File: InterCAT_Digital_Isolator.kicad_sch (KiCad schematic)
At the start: 22 parts, among them U10 MAX3250, U11 EL357N(C)(TA)-G, U12 EL357N(C)(TA)-G, U8 EL357N(C)(TA)-G, U9 EL357N(C)(TA)-G

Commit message: corrected gain of the amplifiers and dyn range, continued PCB
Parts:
- C27, C32: Note X7R -> 50V X7R
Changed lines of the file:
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@@
       (effects (font (size 1.27 1.27)) hide)
     )
-    (property "Note" "X7R" (at 149.86 30.48 0)
+    (property "Note" "50V X7R" (at 149.86 30.48 0)
       (effects (font (size 1.27 1.27)) hide)
     )
@@
       (effects (font (size 1.27 1.27)) hide)
     )
-    (property "Note" "X7R" (at 154.94 30.48 0)
-      (effects (font (size 1.27 1.27)) hide)
-    )
+    (property "Note" "50V X7R" (at 154.94 30.48 0)
+      (effects (font (size 1.27 1.27)) hide)
+    )

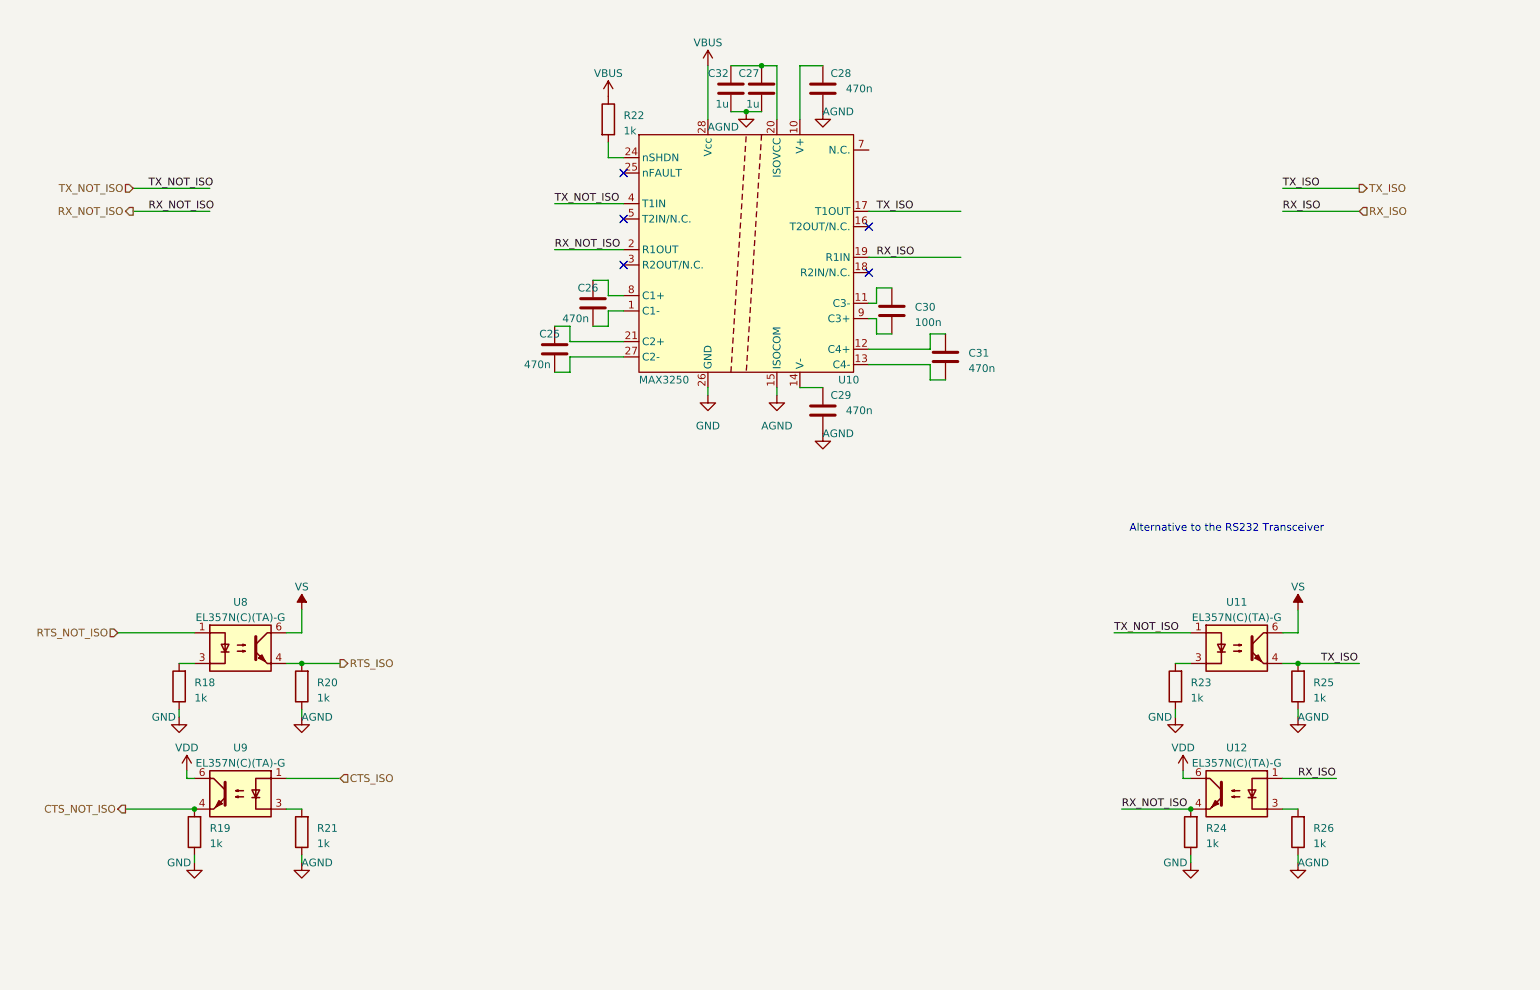
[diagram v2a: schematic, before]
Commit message: Started Version 2.0, migrated to STM32, changed some symbols, added 3V3 Supply
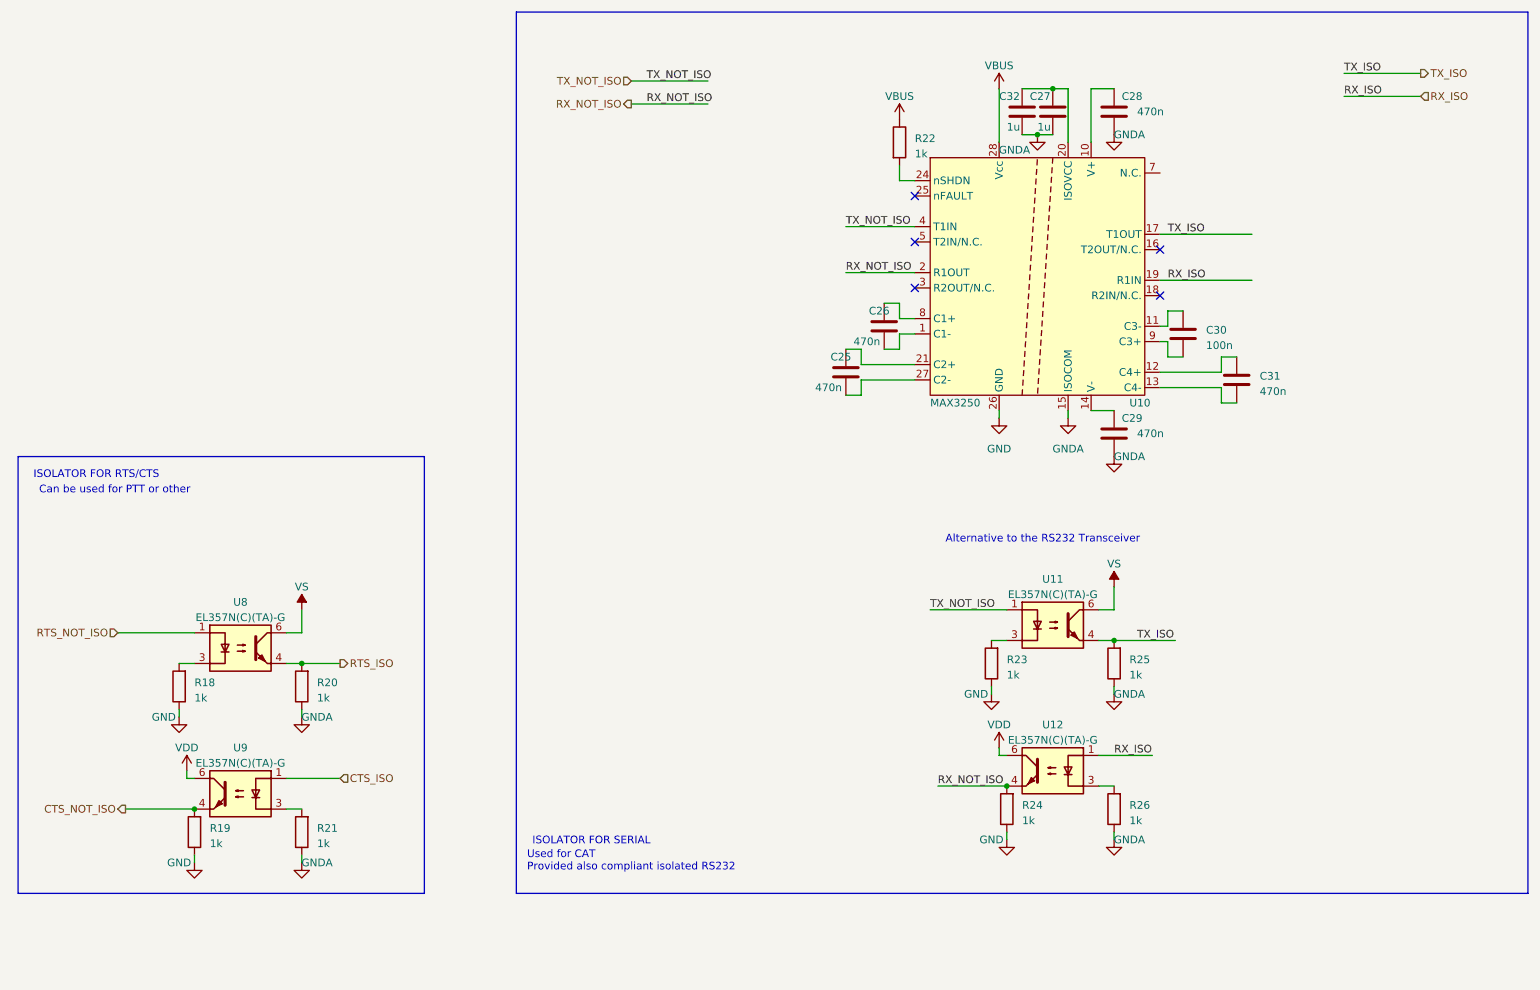
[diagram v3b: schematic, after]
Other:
- note added: "Can be used for PTT or other"
- note added: "ISOLATOR FOR RTS/CTS"
- note added: "ISOLATOR FOR SERIAL"
- note added: "Used for CAT Provided also compliant isolated RS232"
- moved on the sheet: C25, C26, C27, C28, C29, C30, C31, C32, R22, R23, R24, R25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

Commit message: Started work on the PBClayout of the new version
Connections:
- net VDD renamed +3.3V
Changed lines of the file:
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@@
 	(wire
 		(pts
-			(xy 194.31 140.97) (xy 195.58 140.97)
+			(xy 191.77 140.97) (xy 195.58 140.97)
 		)
 		(stroke
@@
 	(wire
 		(pts
-			(xy 59.69 143.51) (xy 59.69 144.78)
+			(xy 58.42 143.51) (xy 58.42 144.78)
 		)
 		(stroke
@@
 	(wire
 		(pts
+			(xy 191.77 139.7) (xy 191.77 140.97)
+		)
+		(stroke
+			(width 0)
+			(type default)
+		)
+	)
+	(wire
+		(pts
 			(xy 210.82 140.97) (xy 219.71 140.97)
 		)
@@
 	(wire
 		(pts
-			(xy 194.31 139.7) (xy 194.31 140.97)
-		)
-		(stroke
-			(width 0)
-			(type default)
-		)
-	)
-	(wire
-		(pts
 			(xy 209.55 39.37) (xy 209.55 30.48)
 		)
@@
 	(wire
 		(pts
-			(xy 59.69 144.78) (xy 60.96 144.78)
+			(xy 58.42 144.78) (xy 60.96 144.78)
 		)
 		(stroke
@@
 	)
 	(symbol
+		(lib_id "power:+3.3V")
+		(at 191.77 139.7 0)
+		(unit 1)
+		(exclude_from_sim no)
+		(in_bom yes)
+		(on_board yes)
+		(dnp no)
+		(fields_autoplaced yes)
+		(property "Reference" "#PWR027"
+			(at 191.77 143.51 0)
+			(effects
+				(font
+					(size 1.27 1.27)
+				)
+				(hide yes)
+			)
+		)
+		(property "Value" "+3.3V"
+			(at 191.77 134.62 0)
+			(effects
+				(font
+					(size 1.27 1.27)
+				)
+			)
+		)
+		(property "Footprint" ""
+			(at 191.77 139.7 0)
+			(effects
+				(font
+					(size 1.27 1.27)
+				)
+				(hide yes)
+			)
+		)
+		(property "Datasheet" ""
+			(at 191.77 139.7 0)
+			(effects
+				(font
+					(size 1.27 1.27)
+				)
+				(hide yes)
+			)
+		)
+		(property "Description" "Power symbol creates a global label with name \"+3.3V\""
+			(at 191.77 139.7 0)
+			(effects
+				(font
+					(size 1.27 1.27)
+				)
+				(hide yes)
+			)
+		)
+		(pin "1"
+		)
+		(instances
+			(project "Intercat"
+				(path "/03d88a85-11fd-47aa-954c-c318bb15294a/fcde6974-78be-43f2-8f1f-c3bd2febfa67"
+					(reference "#PWR027")
+					(unit 1)
+				)
+			)
+		)
+	)
+	(symbol
 		(lib_id "Device:C")
 		(at 224.79 71.12 0)
@@
 	)
 	(symbol
+		(lib_id "power:+3.3V")
+		(at 58.42 143.51 0)
+		(unit 1)
+		(exclude_from_sim no)
+		(in_bom yes)
+		(on_board yes)
+		(dnp no)
+		(fields_autoplaced yes)
+		(property "Reference" "#PWR023"
+			(at 58.42 147.32 0)
+			(effects
+				(font
+					(size 1.27 1.27)
+				)
+				(hide yes)
+			)
+		)
+		(property "Value" "+3.3V"
+			(at 58.42 138.43 0)
+			(effects
+				(font
+					(size 1.27 1.27)
+				)
+			)
+		)
+		(property "Footprint" ""
+			(at 58.42 143.51 0)
+			(effects
+				(font
+					(size 1.27 1.27)
+				)
+				(hide yes)
+			)
+		)
+		(property "Datasheet" ""
+			(at 58.42 143.51 0)
+			(effects
+				(font
+					(size 1.27 1.27)
+				)
+				(hide yes)
+			)
+		)
+		(property "Description" "Power symbol creates a global label with name \"+3.3V\""
+			(at 58.42 143.51 0)
+			(effects
+				(font
+					(size 1.27 1.27)
+				)
+				(hide yes)
+			)
+		)
+		(pin "1"
+		)
+		(instances
+			(project ""
+				(path "/03d88a85-11fd-47aa-954c-c318bb15294a/fcde6974-78be-43f2-8f1f-c3bd2febfa67"
+					(reference "#PWR023")
+					(unit 1)
+				)
+			)
+		)
+	)
+	(symbol
 		(lib_id "Device:C")
 		(at 175.26 69.85 0)
@@
 	)
 	(symbol
-		(lib_id "power:VDD")
-		(at 194.31 139.7 0)
-		(unit 1)
-		(exclude_from_sim no)
-		(in_bom yes)
-		(on_board yes)
-		(dnp no)
-		(property "Reference" "#PWR065"
-			(at 194.31 143.51 0)
-			(effects
-				(font
-					(size 1.27 1.27)
-				)
-				(hide yes)
-			)
-		)
-		(property "Value" "VDD"
-			(at 194.31 135.89 0)
-			(effects
-				(font
-					(size 1.27 1.27)
-				)
-			)
-		)
-		(property "Footprint" ""
-			(at 194.31 139.7 0)
-			(effects
-				(font
-					(size 1.27 1.27)
-				)
-				(hide yes)
-			)
-		)
-		(property "Datasheet" ""
-			(at 194.31 139.7 0)
-			(effects
-				(font
-					(size 1.27 1.27)
-				)
-				(hide yes)
-			)
-		)
-		(property "Description" ""
-			(at 194.31 139.7 0)
-			(effects
-				(font
-					(size 1.27 1.27)
-				)
-			)
-		)
-		(pin "1"
-		)
-		(instances
-			(project "Intercat"
-				(path "/03d88a85-11fd-47aa-954c-c318bb15294a/fcde6974-78be-43f2-8f1f-c3bd2febfa67"
-					(reference "#PWR065")
-					(unit 1)
-				)
-			)
-		)
-	)
-	(symbol
 		(lib_id "power:GNDA")
 		(at 78.74 134.62 0)
@@
 					(unit 1)
 				)
-			)
-		)
-	)
-	(symbol
-		(lib_id "power:VDD")
-		(at 59.69 143.51 0)
-		(unit 1)
-		(exclude_from_sim no)
-		(in_bom yes)
-		(on_board yes)
-		(dnp no)
-		(fields_autoplaced yes)
-		(property "Reference" "#PWR052"
-			(at 59.69 147.32 0)
-			(effects
-				(font
-					(size 1.27 1.27)
-				)
-				(hide yes)
-			)
-		)
-		(property "Value" "VDD"
-			(at 59.69 139.7 0)
-			(effects
-				(font
-					(size 1.27 1.27)
-				)
-			)
-		)
-		(property "Footprint" ""
-			(at 59.69 143.51 0)
-			(effects
-				(font
-					(size 1.27 1.27)
-				)
-				(hide yes)
-			)
-		)
-		(property "Datasheet" ""
-			(at 59.69 143.51 0)
-			(effects
-				(font
-					(size 1.27 1.27)
-				)
-				(hide yes)
-			)
-		)
-		(property "Description" ""
-			(at 59.69 143.51 0)
-			(effects
-				(font
-					(size 1.27 1.27)
-				)
-			)
-		)
-		(pin "1"
-		)
-		(instances
-			(project "Intercat"
-				(path "/03d88a85-11fd-47aa-954c-c318bb15294a/fcde6974-78be-43f2-8f1f-c3bd2febfa67"
-					(reference "#PWR052")
-					(unit 1)
-				)

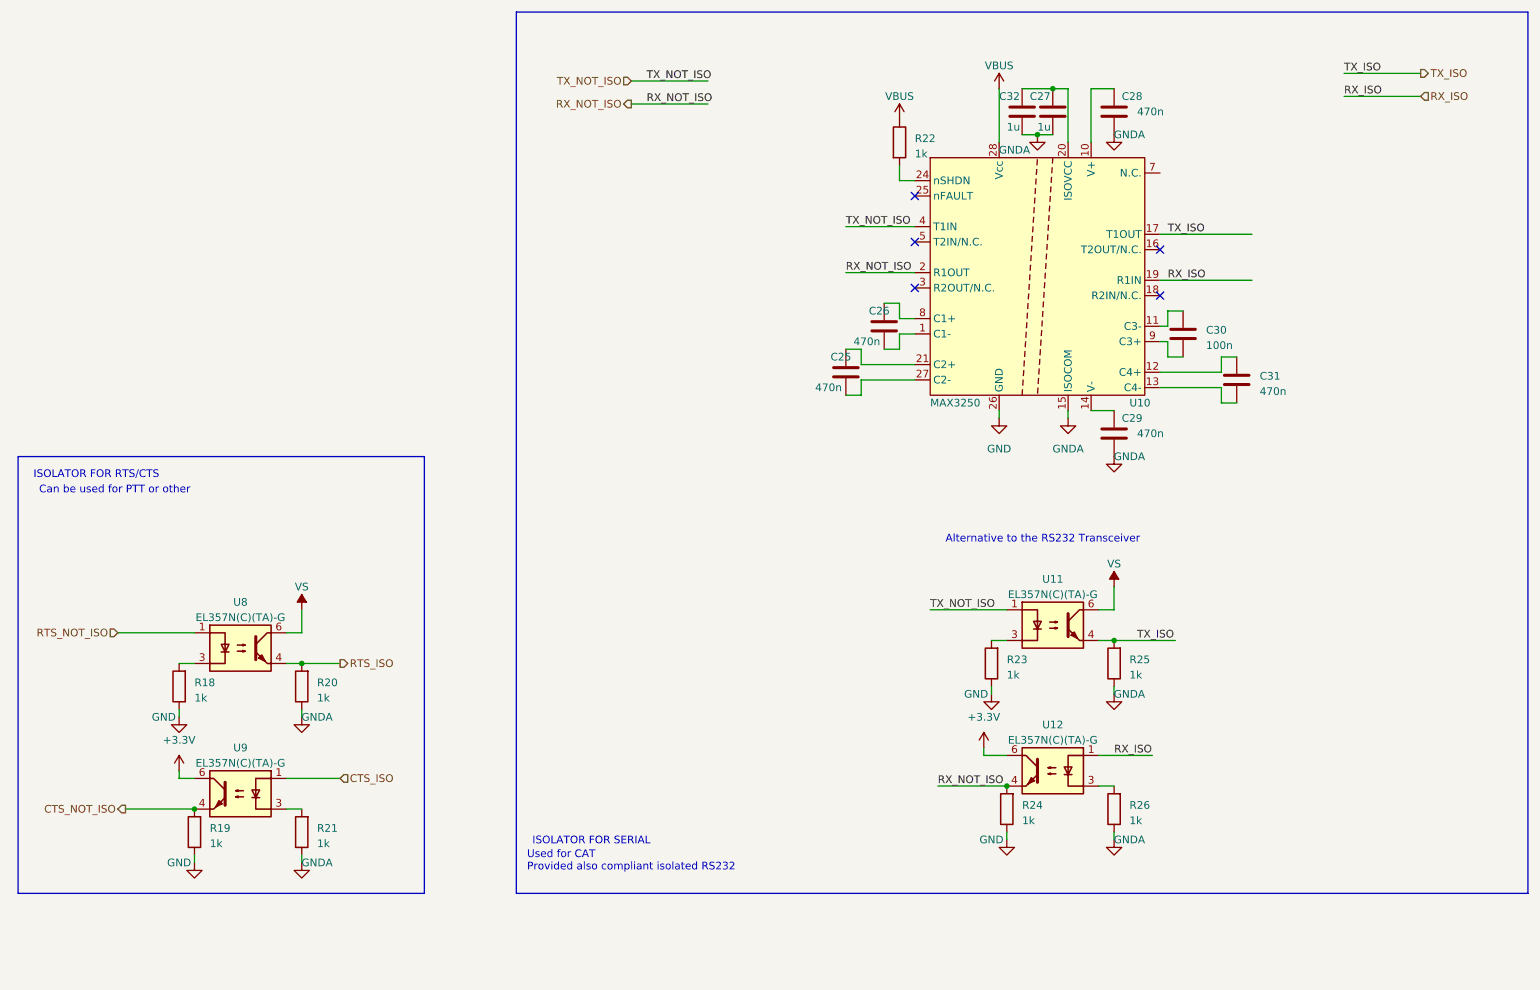
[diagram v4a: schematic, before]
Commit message: added trafo bypass, added zener reg, added todo
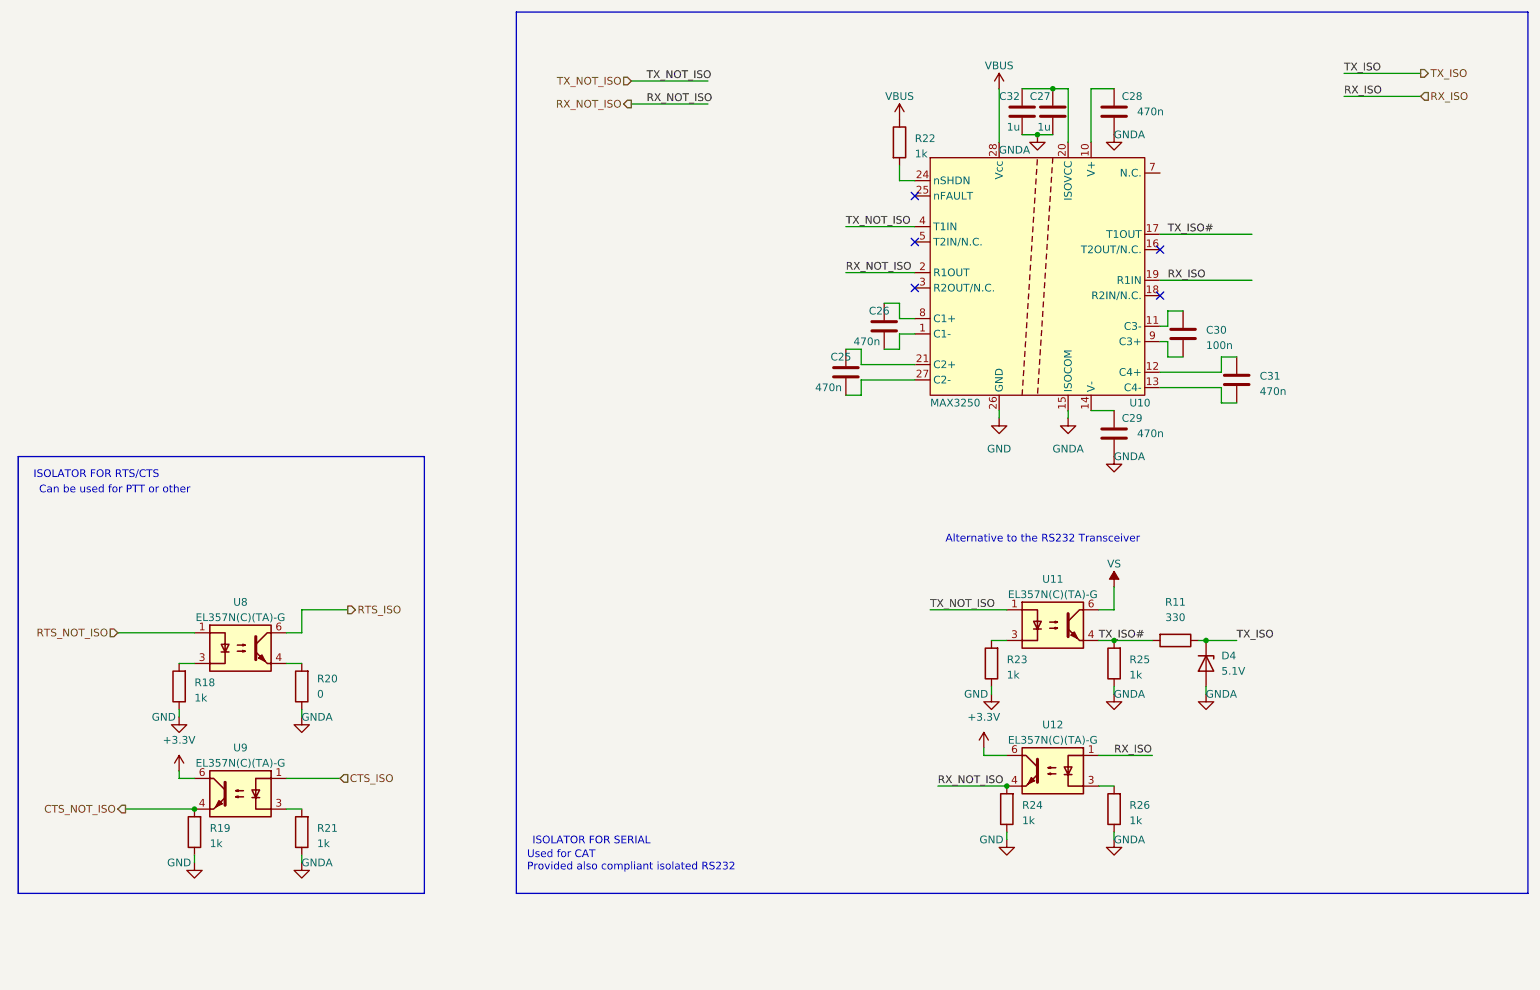
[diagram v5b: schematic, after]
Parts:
- added D4: 5.1V, Diode_SMD:D_0603_1608Metric, symbol Device:D_Zener
- added R11: 330, Resistor_SMD:R_0603_1608Metric, symbol Device:R
- R20: value 1k -> 0; LCSC C21190 -> (none)
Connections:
- net GNDA: now also D4.2 (A)
- net RTS_ISO: now also U8.6; no longer R20.2, U8.4
- net TX_ISO: now also D4.1 (K), R11.1; no longer R25.2, U10.17 (T1OUT), U11.4
- net VS: no longer U8.6
- new net: R20.2, U8.4
- new net TX_ISO#: R11.2, R25.2, U10.17 (T1OUT), U11.4
